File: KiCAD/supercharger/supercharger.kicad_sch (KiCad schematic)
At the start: 24 parts, among them J2 BAT, J3 CALC, J4 UJC-H-G-SMT-1-P6-TR

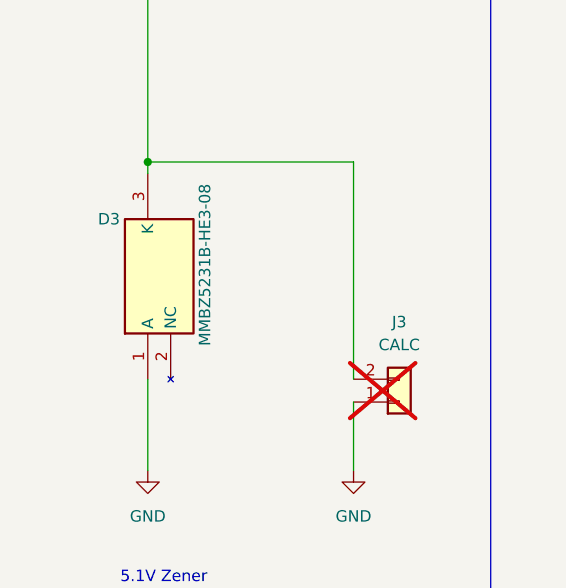
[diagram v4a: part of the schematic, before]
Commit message: Update supercharger with wired interconnect to intercooler.
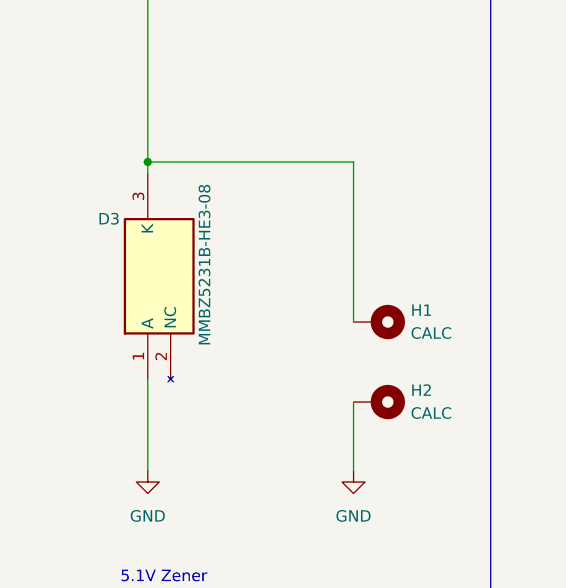
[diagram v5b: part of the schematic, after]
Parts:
- removed J3: CALC, Connector_PinHeader_2.54mm:PinHeader_1x02_P2.54mm_Horizontal, symbol Connector_Generic:Conn_01x02
- added H1, H2: CALC, TestPoint:TestPoint_THTPad_D1.5mm_Drill0.7mm, symbol Mechanical:MountingHole_Pad
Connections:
- net GND: now also H2.1
- net at D2.5 (OUT), D3.3 (K): now also H1.1
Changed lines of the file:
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@@
 	(wire
 		(pts
-			(xy 217.17 55.88) (xy 217.17 80.01)
+			(xy 217.17 55.88) (xy 217.17 73.66)
 		)
 		(stroke
@@
 	)
 	(symbol
-		(lib_id "Connector_Generic:Conn_01x02")
-		(at 222.25 82.55 0)
-		(mirror x)
-		(unit 1)
-		(exclude_from_sim no)
-		(in_bom yes)
-		(on_board yes)
-		(dnp yes)
-		(property "Reference" "J3"
-			(at 222.25 73.66 0)
-			(effects
-				(font
-					(size 1.27 1.27)
-				)
-			)
-		)
-		(property "Value" "CALC"
-			(at 222.25 76.2 0)
-			(effects
-				(font
-					(size 1.27 1.27)
-				)
-			)
-		)
-		(property "Footprint" "Connector_PinHeader_2.54mm:PinHeader_1x02_P2.54mm_Horizontal"
-			(at 222.25 82.55 0)
-			(effects
-				(font
-					(size 1.27 1.27)
-				)
-				(hide yes)
-			)
-		)
-		(property "Datasheet" "~"
-			(at 222.25 82.55 0)
-			(effects
-				(font
-					(size 1.27 1.27)
-				)
-				(hide yes)
-			)
-		)
-		(property "Description" "Generic connector, single row, 01x02, script generated (kicad-library-utils/schlib/autogen/connector/)"
-			(at 222.25 82.55 0)
-			(effects
-				(font
-					(size 1.27 1.27)
-				)
-				(hide yes)
-			)
-		)
-		(pin "1"
-		)
-		(pin "2"
-		)
-		(instances
-			(project "supercharger"
-				(path "/beb21a27-8a6b-49b9-b0ea-25f155128b2e"
-					(reference "J3")
-					(unit 1)
-				)
-			)
-		)
-	)
-	(symbol
 		(lib_id "power:GND")
 		(at 62.23 171.45 0)
@@
 	)
 	(symbol
+		(lib_id "Mechanical:MountingHole_Pad")
+		(at 219.71 82.55 270)
+		(unit 1)
+		(exclude_from_sim yes)
+		(in_bom no)
+		(on_board yes)
+		(dnp no)
+		(fields_autoplaced yes)
+		(property "Reference" "H2"
+			(at 223.52 81.2799 90)
+			(effects
+				(font
+					(size 1.27 1.27)
+				)
+				(justify left)
+			)
+		)
+		(property "Value" "CALC"
+			(at 223.52 83.8199 90)
+			(effects
+				(font
+					(size 1.27 1.27)
+				)
+				(justify left)
+			)
+		)
+		(property "Footprint" "TestPoint:TestPoint_THTPad_D1.5mm_Drill0.7mm"
+			(at 219.71 82.55 0)
+			(effects
+				(font
+					(size 1.27 1.27)
+				)
+				(hide yes)
+			)
+		)
+		(property "Datasheet" "~"
+			(at 219.71 82.55 0)
+			(effects
+				(font
+					(size 1.27 1.27)
+				)
+				(hide yes)
+			)
+		)
+		(property "Description" "Mounting Hole with connection"
+			(at 219.71 82.55 0)
+			(effects
+				(font
+					(size 1.27 1.27)
+				)
+				(hide yes)
+			)
+		)
+		(pin "1"
+		)
+		(instances
+			(project "supercharger"
+				(path "/beb21a27-8a6b-49b9-b0ea-25f155128b2e"
+					(reference "H2")
+					(unit 1)
+				)
+			)
+		)
+	)
+	(symbol
 		(lib_id "Device:R")
 		(at 33.02 76.2 0)
@@
 					(unit 1)
 				)
+			)
+		)
+	)
+	(symbol
+		(lib_id "Mechanical:MountingHole_Pad")
+		(at 219.71 73.66 270)
+		(unit 1)
+		(exclude_from_sim yes)
+		(in_bom no)
+		(on_board yes)
+		(dnp no)
+		(fields_autoplaced yes)
+		(property "Reference" "H1"
+			(at 223.52 72.3899 90)
+			(effects
+				(font
+					(size 1.27 1.27)
+				)
+				(justify left)
+			)
+		)
+		(property "Value" "CALC"
+			(at 223.52 74.9299 90)
+			(effects
+				(font
+					(size 1.27 1.27)
+				)
+				(justify left)
+			)
+		)
+		(property "Footprint" "TestPoint:TestPoint_THTPad_D1.5mm_Drill0.7mm"
+			(at 219.71 73.66 0)
+			(effects
+				(font
+					(size 1.27 1.27)
+				)
+				(hide yes)
+			)
+		)
+		(property "Datasheet" "~"
+			(at 219.71 73.66 0)
+			(effects
+				(font
+					(size 1.27 1.27)
+				)
+				(hide yes)
+			)
+		)
+		(property "Description" "Mounting Hole with connection"
+			(at 219.71 73.66 0)
+			(effects
+				(font
+					(size 1.27 1.27)
+				)
+				(hide yes)
+			)
+		)
+		(pin "1"
+		)
+		(instances
+			(project ""
+				(path "/beb21a27-8a6b-49b9-b0ea-25f155128b2e"
+					(reference "H1")
+					(unit 1)
+				)
